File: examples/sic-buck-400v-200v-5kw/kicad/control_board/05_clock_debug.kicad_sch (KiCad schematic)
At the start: 17 parts, among them J3 J_JTAG: TI 14-pin, key pin 6 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, J4 J_BOOT: jumper 1-2 = SCI-A bo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, J5 J_UART: SCI-A, 3.3 V levels o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, Y1 ASV-30.000MHZ-EJ-T

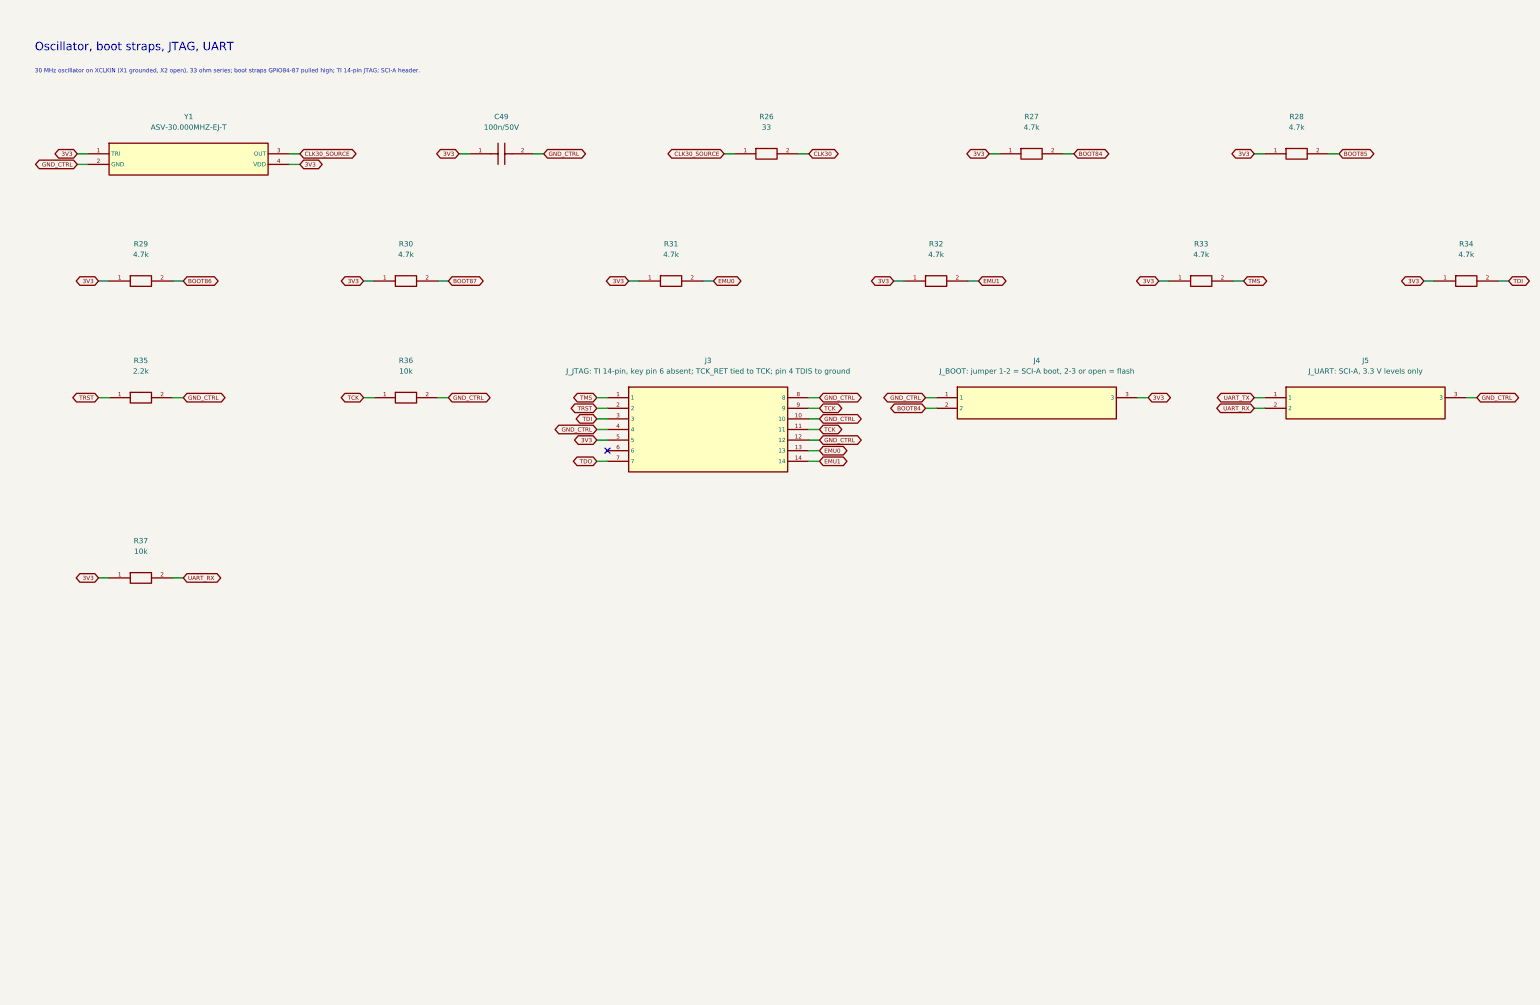
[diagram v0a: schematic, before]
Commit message: feat(v2.1): example regenerated - wired schematics, both boards routed with the upgraded router, exports, crops, validation
Schematics (wired style, gates passed): ERC 0 on both projects (power 20261012T075113Z-erc-df18ce6e,
control 20261012T075120Z-erc-7a14cacb); netlist (ref,pad)->net exact vs the model and vs the frozen V2
netlists with equal net names; .kicad_dru / net_settings identical to the legacy generation; stub
global labels 648 -> 7 (power) and 667 -> 7 (control), wired pin share 0 -> 0.90 / 0.76, junctions,
hierarchical labels and power symbols introduced, continuation sheets removed; readability metrics
V2 vs V2.1 in engineering_checks/schematic_readability_*.

Power board (octilinear simplification + tangent arcs on the V2 search; 8-direction search kept
opt-in after attempt A left 2 connections open): 0 unresolved, DRC 0/0/0 (20261012T090308Z-drc-8fd50803),
segments 4755 -> 2991 + 145 arcs, 90-degree bends 3609 -> 1121, stair runs 382 -> 124, length
5744.6 -> 5545.6 mm, vias 606 = V2, no net longer / more vias / narrower. Control board: 0 unresolved,
DRC 0/0/0 (20261012T084327Z-drc-7f07f983), segments 5995 -> 4262 + 261 arcs, 90-degree bends
4069 -> 1233, stair runs 435 -> 144, length 7055.2 -> 6700.7 mm, vias 798 = V2, 96 nets shorter,
0 longer. FOOTPRINT.SetDNP for DNP parts (schematic parity), beautify anchors bound to off-grid vias
by copper overlap (path_geometry.connected_by_overlap), In2.Cu inner pass styled.

Exports 11/11 per board, renders and layer PDFs refreshed, high-resolution V2/V2.1 crops under
review/crops/, routing_quality_* and v21_validation.{json,md} (nine TASK 7 checks independently
re-derived). verify_sic_buck passed; 338 tests OK (2 skipped).

Co-Authored-By: Claude Fable 5.1 <noreply@anthropic.com>
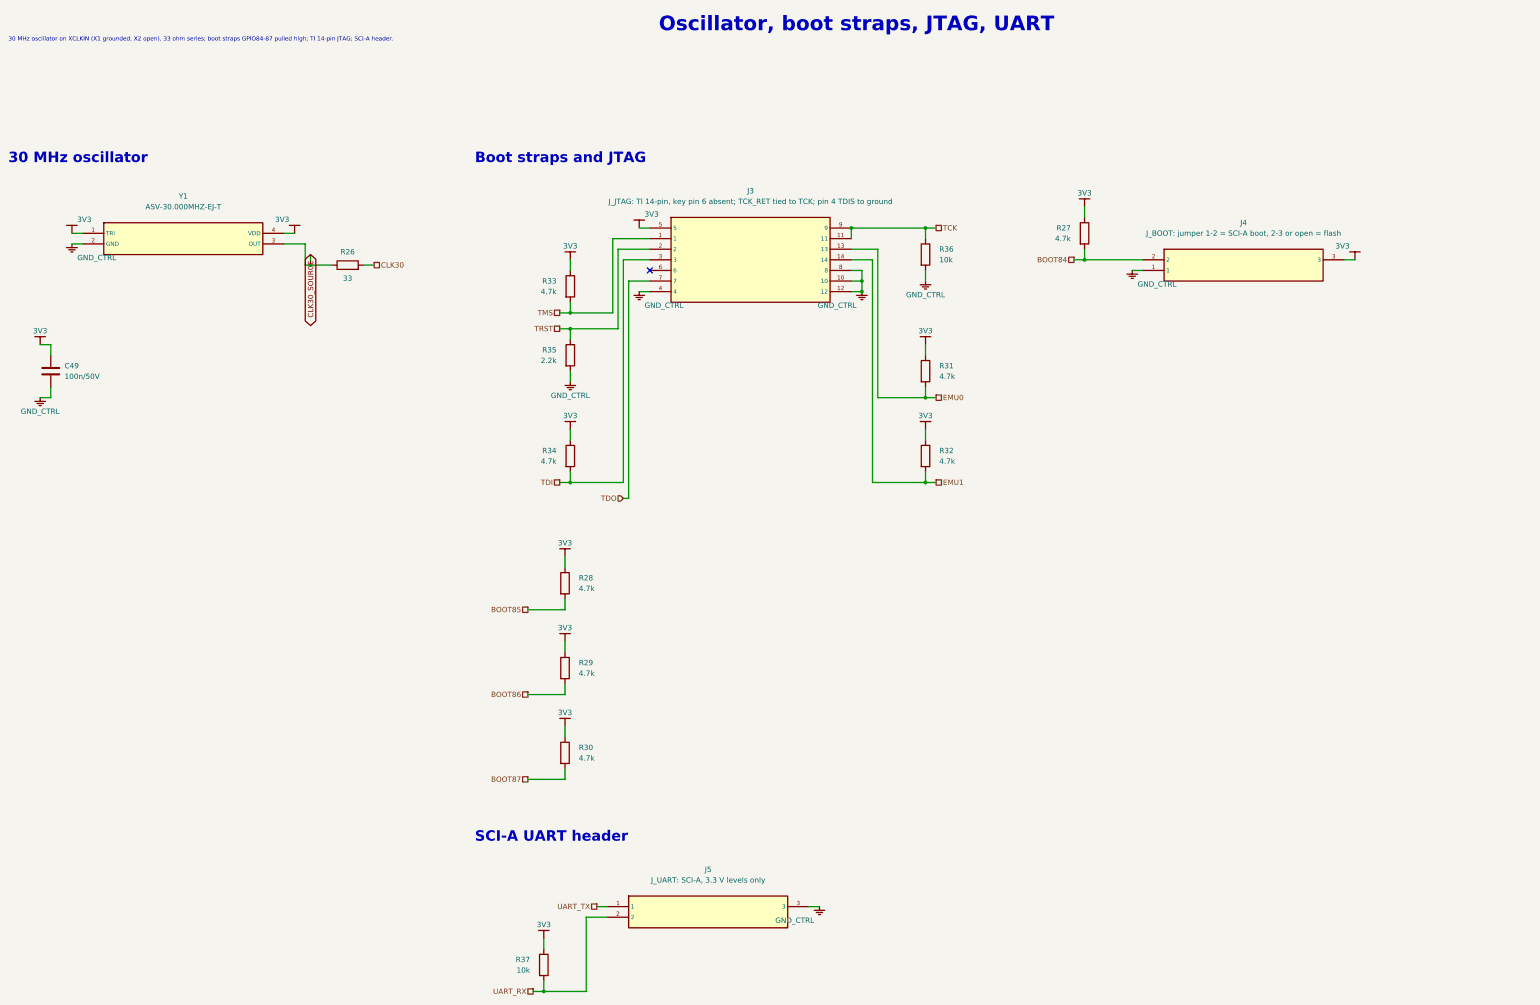
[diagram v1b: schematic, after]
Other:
- note added: "30 MHz oscillator"
- note added: "Boot straps and JTAG"
- note added: "SCI-A UART header"
- moved on the sheet: J3, J4, J5, Y1
